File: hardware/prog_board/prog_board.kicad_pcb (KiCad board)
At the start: 2 copper layers, 16 parts, among them J1 USB_OTG, J2 Conn_02x03_Odd_Even, Q1 MMBT2222, Q2 MMBT2222, SW1 SW_Push, U1 CP2104

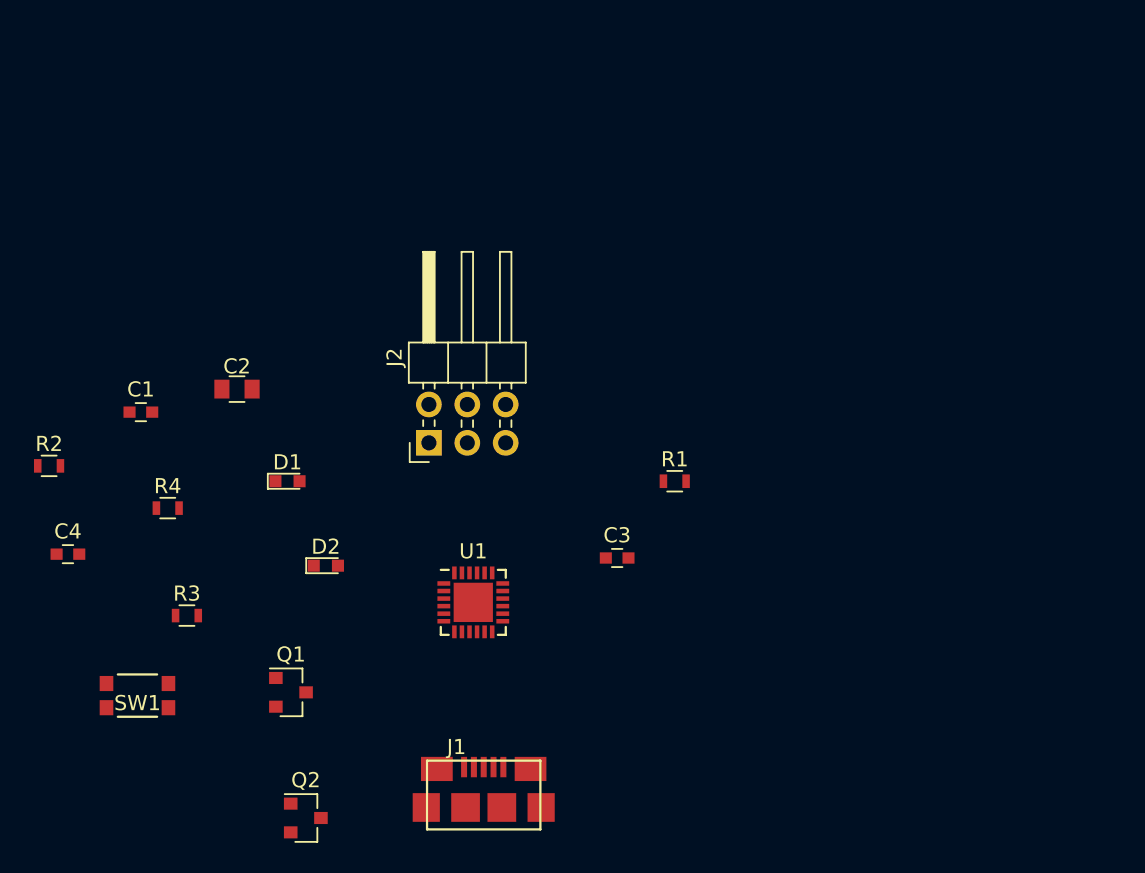
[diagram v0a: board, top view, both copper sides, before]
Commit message: Changed board size to use with new tubes
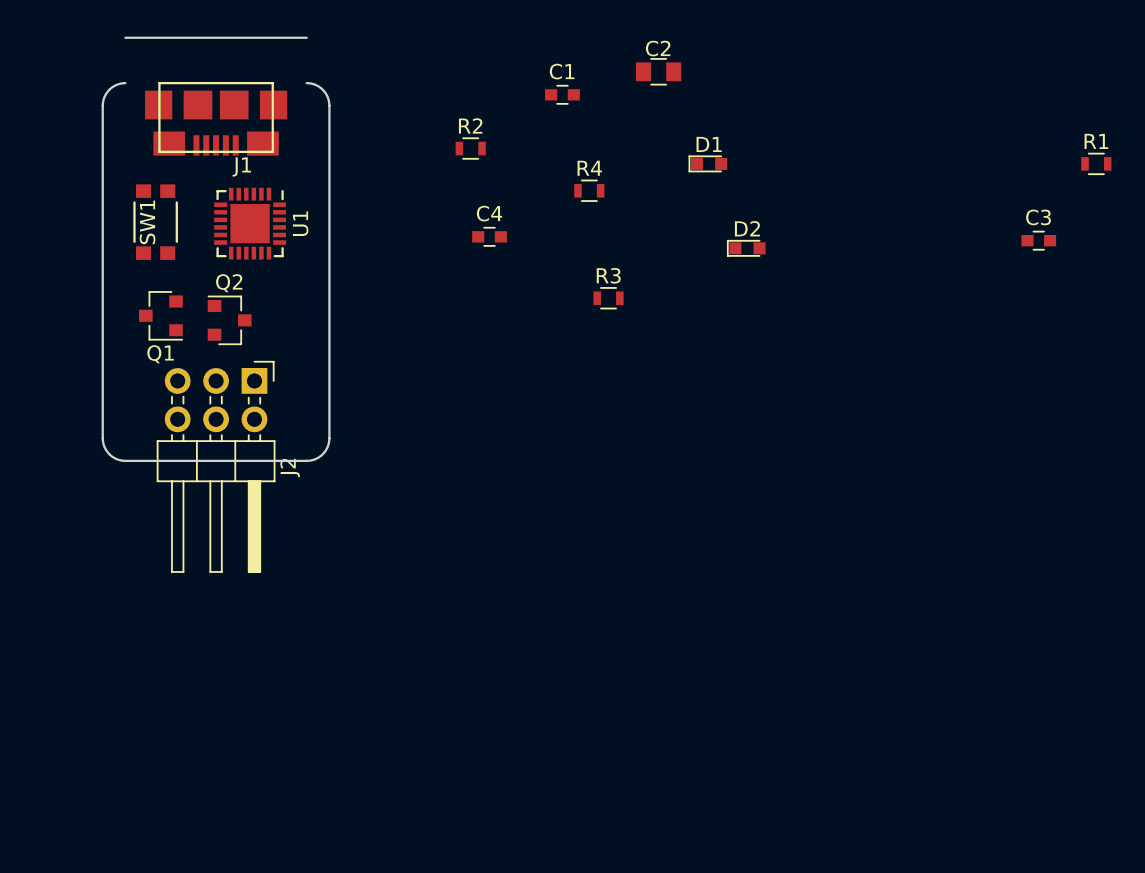
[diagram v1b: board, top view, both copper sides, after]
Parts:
- moved J1 52.5 mm to (150.0, 75.0), turned to 180 degrees
- moved C1 34.9 mm to (172.9, 75.8)
- moved C2 34.9 mm to (179.3, 74.2)
- moved C3 34.9 mm to (204.4, 85.4)
- moved C4 34.9 mm to (168.1, 85.2)
- moved D1 34.9 mm to (182.6, 80.3)
- moved R1 34.9 mm to (208.3, 80.3)
- moved R2 34.9 mm to (166.8, 79.3)
- moved R3 34.9 mm to (176.0, 89.2)
- moved D2 34.9 mm to (185.2, 85.9)
- moved R4 34.9 mm to (174.7, 82.1)
- moved Q2 33.3 mm to (150.9, 90.7)
- moved SW1 31.4 mm to (146.0, 84.2), turned to 270 degrees
- moved U1 29.1 mm to (152.2, 84.3), turned to 270 degrees
- moved Q1 26.4 mm to (146.3, 90.4), turned to 180 degrees
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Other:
- board outline added: 15 x 28 mm

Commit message: Working on layout
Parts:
- J2: moved to B.Cu
- moved R1 57.0 mm to (151.9, 89.1), turned to 180 degrees
- moved C3 56.3 mm to (148.2, 82.7), turned to 270 degrees
- moved D2 41.0 mm to (144.6, 91.6), turned to 180 degrees
- moved D1 38.9 mm to (144.6, 88.4), turned to 180 degrees
- moved R3 31.5 mm to (144.6, 86.8), turned to 180 degrees
- moved R4 31.1 mm to (144.6, 90.0), turned to 180 degrees
- moved C2 25.3 mm to (154.4, 78.6)
- moved C1 23.0 mm to (150.1, 78.9), turned to 180 degrees
- moved R2 19.0 mm to (151.9, 91.1)
- moved C4 16.4 mm to (151.8, 86.6), turned to 180 degrees
- moved Q1 8.86 mm to (155.2, 90.1), turned to 0 degrees
- moved J2 5.08 mm to (147.5, 94.8)
- moved J1 3.00 mm to (150.0, 72.0)
- moved SW1 2.77 mm to (144.8, 81.7)
- moved Q2 2.38 mm to (148.6, 90.1), turned to 180 degrees
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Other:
- outline, holes or cut-outs redrawn

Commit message: Working on layout
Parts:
- moved C2 7.02 mm to (147.5, 79.9), turned to 90 degrees
- moved C3 1.00 mm to (148.2, 83.7)
- moved SW1 0.63 mm to (144.6, 82.3)
- moved U1 0.30 mm to (152.6, 82.7)
- moved C1 0.14 mm to (150.2, 78.8)
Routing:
- net Net-(J1-Pad3): track 0.00 -> 6.86 mm, vias 0 -> 2
- net Net-(J1-Pad2): track 0.00 -> 5.33 mm
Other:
- net class Default: clearance 0.2 -> 0.1524; trace_width 0.25 -> 0.1524; via_dia 0.6 -> 0.452; via_drill 0.4 -> 0.3
- rule trace_clearance: 0.2 -> 0.1524
- rule trace_min: 0.2 -> 0.1524
- rule via_min_size: 0.4 -> 0.452
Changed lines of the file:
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@@
     (links 45)
     (no_connects 45)
-    (area 142.424999 71.924999 157.575001 100.075001)
-    (thickness 1.6)
+    (area 142.424999 71.61 159.268572 109.007382)
+    (thickness 1.2)
     (drawings 8)
-    (tracks 0)
+    (tracks 11)
     (zones 0)
     (modules 16)
@@
     (0 F.Cu signal)
     (31 B.Cu signal)
-    (32 B.Adhes user hide)
-    (33 F.Adhes user hide)
     (34 B.Paste user hide)
     (35 F.Paste user hide)
@@
     (38 B.Mask user hide)
     (39 F.Mask user hide)
-    (40 Dwgs.User user hide)
-    (41 Cmts.User user hide)
-    (42 Eco1.User user hide)
-    (43 Eco2.User user hide)
     (44 Edge.Cuts user)
-    (45 Margin user hide)
-    (46 B.CrtYd user hide)
-    (47 F.CrtYd user hide)
-    (48 B.Fab user hide)
-    (49 F.Fab user hide)
+    (46 B.CrtYd user)
+    (47 F.CrtYd user)
   )
   (setup
-    (last_trace_width 0.25)
-    (trace_clearance 0.2)
+    (last_trace_width 0.1524)
+    (user_trace_width 0.2)
+    (user_trace_width 0.3)
+    (trace_clearance 0.1524)
     (zone_clearance 0.508)
     (zone_45_only no)
-    (trace_min 0.2)
+    (trace_min 0.1524)
     (segment_width 0.2)
     (edge_width 0.15)
-    (via_size 0.6)
-    (via_drill 0.4)
-    (via_min_size 0.4)
+    (via_size 0.452)
+    (via_drill 0.3)
+    (via_min_size 0.452)
     (via_min_drill 0.3)
-    (uvia_size 0.3)
-    (uvia_drill 0.1)
+    (user_via 0.452 0.3)
+    (uvia_size 0.452)
+    (uvia_drill 0.3)
     (uvias_allowed no)
-    (uvia_min_size 0.2)
-    (uvia_min_drill 0.1)
+    (uvia_min_size 0.452)
+    (uvia_min_drill 0.3)
     (pcb_text_width 0.3)
     (pcb_text_size 1.5 1.5)
@@
   (net 30 "Net-(U1-Pad24)")
   (net_class Default "This is the default net class."
-    (clearance 0.2)
-    (trace_width 0.25)
-    (via_dia 0.6)
-    (via_drill 0.4)
-    (uvia_dia 0.3)
-    (uvia_drill 0.1)
+    (clearance 0.1524)
+    (trace_width 0.1524)
+    (via_dia 0.452)
+    (via_drill 0.3)
+    (uvia_dia 0.452)
+    (uvia_drill 0.3)
     (add_net +3V3)
     (add_net +5V)
@@
   )
   (module Capacitors_SMD:C_0603 (layer F.Cu)
-    (at 150.1 78.9 180)
+    (at 150.2 78.8 180)
     (descr "Capacitor SMD 0603, reflow soldering, AVX (see smccp.pdf)")
     (tags "capacitor 0603")
@@
   )
   (module Capacitors_SMD:C_0805 (layer F.Cu)
-    (at 154.4 78.6)
+    (at 147.5 79.9 90)
     (descr "Capacitor SMD 0805, reflow soldering, AVX (see smccp.pdf)")
     (tags "capacitor 0805")
     (attr smd)
-    (fp_text reference C2 (at 0 -1.5) (layer F.SilkS)
-      (effects (font (size 1 1) (thickness 0.15)))
-    )
-    (fp_text value 10u (at 0 1.75) (layer F.Fab)
-      (effects (font (size 1 1) (thickness 0.15)))
-    )
-    (fp_text user %R (at 0 -1.5) (layer F.Fab)
+    (fp_text reference C2 (at 0 -1.5 90) (layer F.SilkS)
+      (effects (font (size 1 1) (thickness 0.15)))
+    )
+    (fp_text value 10u (at 0 1.75 90) (layer F.Fab)
+      (effects (font (size 1 1) (thickness 0.15)))
+    )
+    (fp_text user %R (at 0 -1.5 90) (layer F.Fab)
       (effects (font (size 1 1) (thickness 0.15)))
     )
@@
     (fp_line (start 1.75 0.87) (end 1.75 -0.88) (layer F.CrtYd) (width 0.05))
     (fp_line (start 1.75 0.87) (end -1.75 0.87) (layer F.CrtYd) (width 0.05))
-    (pad 1 smd rect (at -1 0) (size 1 1.25) (layers F.Cu F.Paste F.Mask)
+    (pad 1 smd rect (at -1 0 90) (size 1 1.25) (layers F.Cu F.Paste F.Mask)
       (net 2 +3V3))
-    (pad 2 smd rect (at 1 0) (size 1 1.25) (layers F.Cu F.Paste F.Mask)
+    (pad 2 smd rect (at 1 0 90) (size 1 1.25) (layers F.Cu F.Paste F.Mask)
       (net 1 GND))
     (model Capacitors_SMD.3dshapes/C_0805.wrl
@@
   )
   (module Capacitors_SMD:C_0603 (layer F.Cu)
-    (at 148.2 82.7 270)
+    (at 148.2 83.7 270)
     (descr "Capacitor SMD 0603, reflow soldering, AVX (see smccp.pdf)")
     (tags "capacitor 0603")
@@
   )
   (module footprint:KMR7 (layer F.Cu)
-    (at 144.8 81.7 270)
+    (at 144.6 82.3 270)
     (fp_text reference SW1 (at 0 0.5 270) (layer F.SilkS)
       (effects (font (size 1 1) (thickness 0.15)))
@@
   )
   (module Housings_DFN_QFN:QFN-24-1EP_4x4mm_Pitch0.5mm (layer F.Cu)
-    (at 152.3 82.7 270)
+    (at 152.6 82.7 270)
     (descr "24-Lead Plastic Quad Flat, No Lead Package (MJ) - 4x4x0.9 mm Body [QFN]; (see Microchip Packaging Specification 00000049BS.pdf)")
     (tags "QFN 0.5")
@@
   (gr_line (start 157.5 98.5) (end 157.5 73.5) (layer Edge.Cuts) (width 0.15))
   (gr_line (start 144 100) (end 156 100) (layer Edge.Cuts) (width 0.15))
+  (segment (start 150.65 76.125) (end 150.65 77.05) (width 0.1524) (layer F.Cu) (net 9))
+  (segment (start 150.65 77.05) (end 152.35 78.75) (width 0.1524) (layer F.Cu) (net 9))
+  (segment (start 152.35 78.75) (end 152.35 80.1726) (width 0.1524) (layer F.Cu) (net 9))
+  (segment (start 152.35 80.1726) (end 152.35 80.75) (width 0.1524) (layer F.Cu) (net 9))
+  (segment (start 152.2 77.6) (end 152.85 78.25) (width 0.1524) (layer F.Cu) (net 10))
+  (segment (start 152.85 78.25) (end 152.85 80.75) (width 0.1524) (layer F.Cu) (net 10))
+  (segment (start 150.4 77.6) (end 152.2 77.6) (width 0.1524) (layer B.Cu) (net 10))
+  (via (at 152.2 77.6) (size 0.452) (drill 0.3) (layers F.Cu B.Cu) (net 10))
+  (segment (start 150 76.125) (end 150 77.2) (width 0.1524) (layer F.Cu) (net 10))
+  (segment (start 150 77.2) (end 150.4 77.6) (width 0.1524) (layer F.Cu) (net 10))
+  (via (at 150.4 77.6) (size 0.452) (drill 0.3) (layers F.Cu B.Cu) (net 10))
 )

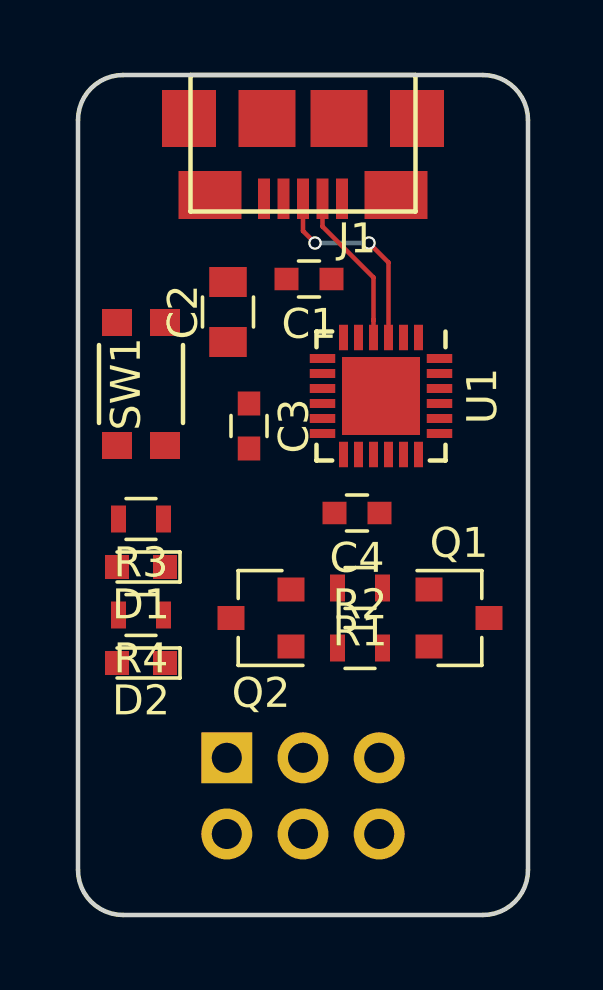
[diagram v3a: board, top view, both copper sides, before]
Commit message: Finished routing programming board
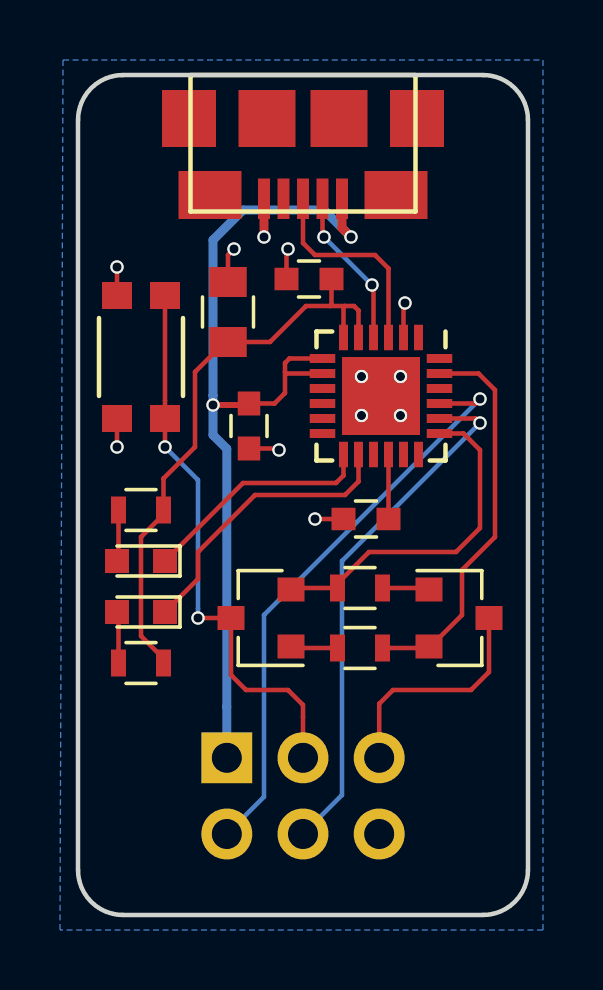
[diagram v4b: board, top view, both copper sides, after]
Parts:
- moved R3 4.80 mm to (144.6, 91.6)
- moved R4 3.50 mm to (144.6, 86.5)
- moved D2 3.40 mm to (144.6, 88.2)
- moved D1 1.50 mm to (144.6, 89.9)
- moved SW1 0.90 mm to (144.6, 81.4)
- moved C4 0.36 mm to (152.1, 86.8)
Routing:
- net +5V: track 0.00 -> 30.4 mm, vias 0 -> 2
- net +3V3: track 0.00 -> 20.1 mm
- net /TXD: track 0.00 -> 19.4 mm, vias 0 -> 1
- net /RESET: track 0.00 -> 18.8 mm, vias 0 -> 2
- net /RXD: track 0.00 -> 17.6 mm, vias 0 -> 1
- net /DTR: track 0.00 -> 13.1 mm
- net /RTS: track 0.00 -> 11.4 mm
- net Net-(D1-Pad1): track 0.00 -> 9.68 mm
- net GND: track 0.00 -> 8.52 mm, vias 0 -> 12
- net Net-(D2-Pad1): track 0.00 -> 7.83 mm
- net /GPIO0: track 0.00 -> 7.70 mm
- net Net-(C4-Pad1): track 0.00 -> 2.15 mm
- net Net-(D2-Pad2): track 0.00 -> 1.72 mm
- net Net-(D1-Pad2): track 0.00 -> 1.72 mm
- net Net-(Q2-Pad1): track 0.00 -> 1.57 mm
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- added copper zone on B.Cu, net GND
